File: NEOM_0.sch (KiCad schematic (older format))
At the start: 20 parts, among them U1 LM3940, U2 7_Pins_Header_PA0_PA6, U3 Reset Button, U4 STM32F070F6P6, U6 7_Pins_Header_PA7_PA14, U7 TPD4S012DRYR, U8 16Mhz, U9 USB_Micro_B

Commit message: Updated the PCB unconnected GND pad..
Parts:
- C1: Digi-Key Part Number	 311-1136-1-ND -> (none); DigiKeyPartNumber	 (none) -> 311-1136-1-ND; Manufacturer Part Number	 CC0805KRX7R9BB103 -> (none); ManufacturerPartNumber	 (none) -> CC0805KRX7R9BB103
- C2: Digi-Key Part Number	 490-1691-1-ND -> (none); DigiKeyPartNumber	 (none) -> 490-1691-1-ND; Manufacturer Part Number	 GRM21BR71C105KA01L -> (none); ManufacturerPartNumber	 (none) -> GRM21BR71C105KA01L
- C3: DigiKeyPartNumber (none) -> 490-8319-1-ND; ManufacturerPartNumber	 (none) -> GRM21BR71H474KA88K
- C4: DigiKeyPartNumber	 (none) -> 445-5986-1-ND; ManufacturerPartNumber	 (none) -> C2012X5R0J336M125AC
- C5: Digi-Key Part Number	 478-1395-1-ND -> (none); DigiKeyPartNumber	 (none) -> 478-1395-1-ND; Manufacturer Part Number	 08055C104KAT2A -> (none); ManufacturerPartNumber	 (none) -> 08055C104KAT2A
- D1: Digi-Key Part Number	 67-1557-1-ND -> (none); DigiKeyPartNumber	 (none) -> 67-1557-1-ND; Manufacturer Part Number	 SML-LXR85GC-TR -> (none); ManufacturerPartNumber	 (none) -> SML-LXR85GC-TR
- R1, R4: Digi-Key Part Number	 311-680ARCT-ND -> (none); DigiKeyPartNumber	 (none) -> 311-680ARCT-ND; Manufacturer Part Number	 RC0805JR-07680RL -> (none); ManufacturerPartNumber	 (none) -> RC0805JR-07680RL
- R2: Digi-Key Part Number	 311-100KCRCT-ND -> (none); DigiKeyPartNumber	 (none) -> 311-100KCRCT-ND; Manufacturer Part Number	 RC0805FR-07100KL -> (none); ManufacturerPartNumber	 (none) -> RC0805FR-07100KL
- R3: DigiKeyPartNumber	 (none) -> 311-100KCRCT-ND; ManufacturerPartNumber	 (none) -> RC0805FR-07100KL
- U1: Digi-Key Part Number	 LM3940IMPX-3.3/NOPBCT-ND -> (none); DigiKeyPartNumber	 (none) -> LM3940IMPX-3.3/NOPBCT-ND; Manufacturer Part Number	 LM3940IMPX-3.3/NOPB -> (none); ManufacturerPartNumber	 (none) -> LM3940IMPX-3.3/NOPB
- U2, U6: DigiKeyPartNumber	 (none) -> S1011EC-07-ND; ManufacturerPartNumber	 (none) -> PRPC007SAAN-RC
- U3: Digi-Key Part Number	 EG5353CT-ND -> (none); DigiKeyPartNumber	 (none) -> EG5353CT-ND; Manufacturer Part Number	 TL3305AF260QG -> (none); ManufacturerPartNumber	 (none) -> TL3305AF260QG
- U4: DigiKeyPartNumber	 (none) -> 497-17353-ND; Manufacturer Part Number	 STM32F070F6P6 -> (none); ManufacturerPartNumber	 (none) -> STM32F070F6P6
- U7: DigiKeyPartNumber	 (none) -> 296-24244-1-ND; ManufacturerPartNumber	 (none) -> TPD4S012DRYR
- U8: Digi-Key Part Number	 490-1198-1-ND -> (none); DigiKeyPartNumber	 (none) -> 490-1198-1-ND; Manufacturer Part Number	 CSTCE16M0V53-R0 -> (none); ManufacturerPartNumber	 (none) -> CSTCE16M0V53-R0
- U9: Digi-Key Part Number	 609-4613-1-ND -> (none); DigiKeyPartNumber	 (none) -> 609-4613-1-ND; Manufacturer Part Number	 10118192-0001LF -> (none); ManufacturerPartNumber	 (none) -> 10118192-0001LF

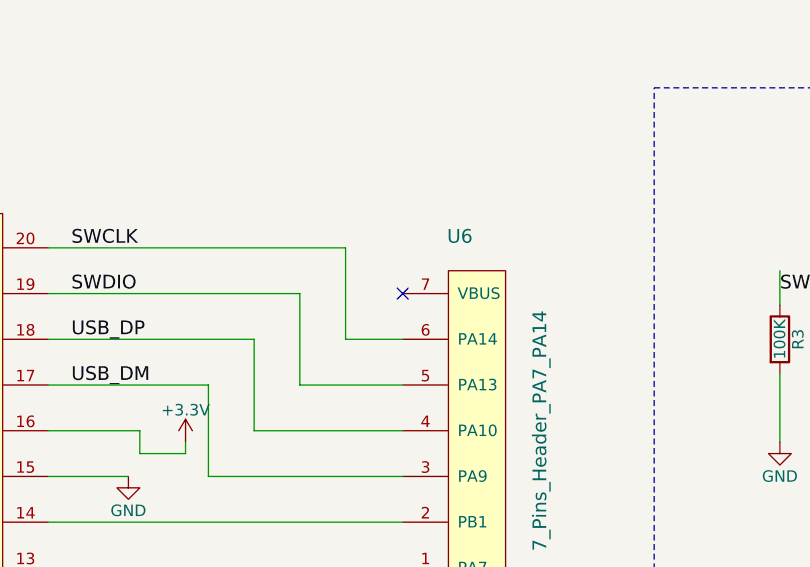
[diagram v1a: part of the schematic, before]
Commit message: Added BAT pin for external battery board..
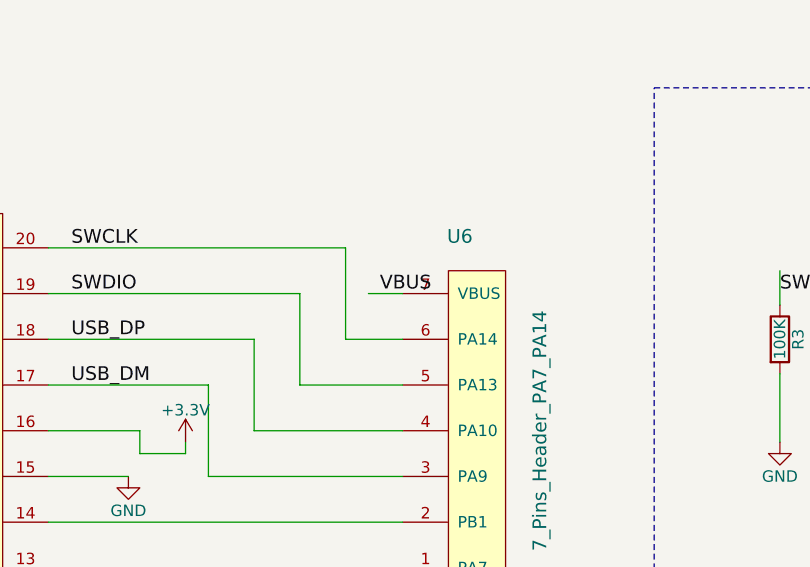
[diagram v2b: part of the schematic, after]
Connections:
- wire segments 88 -> 89
- no-connect marks 2 -> 1
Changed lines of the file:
@@
 Wire Wire Line
 	3350 1400 3200 1400
-NoConn ~ 7800 4200
 $Comp
 L GND #PWR03
@@
 30 3C 9B 92 CF 24 8B DA 51 CD 00 08 DC F9 E9 26 3C 0B 73 01 9F 70 E9 91 80 E7 1F EE EB 72 BD E0
 B4 B1 05 AB 63 DF 09 55 27 EC D5 B5 FC BD 3F 9C 4A 7F 61 62 A3 F8 70 39 5F DC B1 1B B9 9B 02 E2
-5E F0 7F E6 B1 8C 44 57 10 5F 27 00 00 00 00 49 45 4E 44 AE 42 60 82 A3
+5E F0 7F E6 B1 8C 44 57 10 5F 27 00 00 00 00 49 45 4E 44 AE 42 60 82 00
 EndData
 $EndBitmap
@@
 Text Label 9400 1900 1    60   ~ 0
 USB_DM
+Text Label 7700 4200 0    60   ~ 0
+VBUS
+Wire Wire Line
+	7800 4200 7650 4200
 $EndSCHEMATC

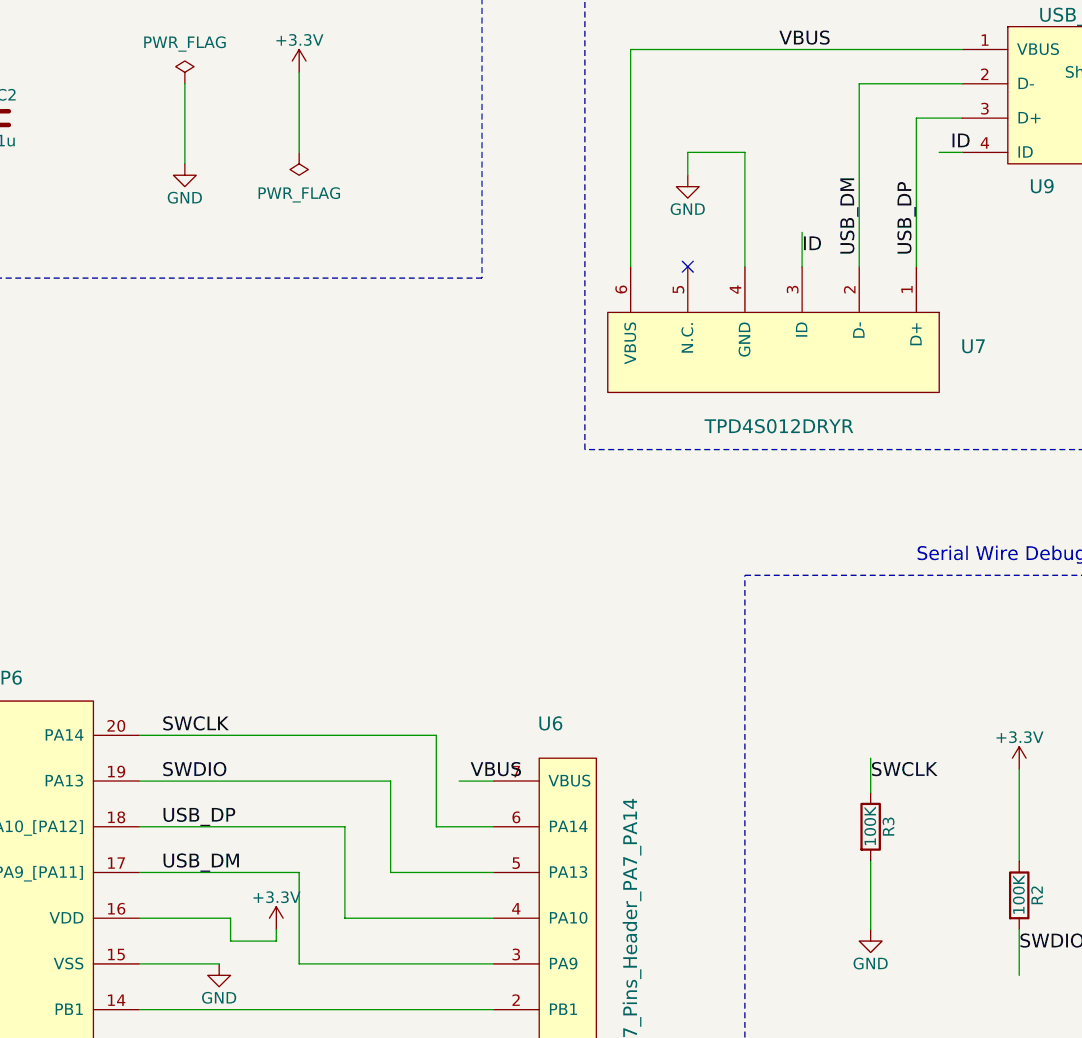
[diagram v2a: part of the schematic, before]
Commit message: Updated PCB: added defferintial pair routing to USB+/-...
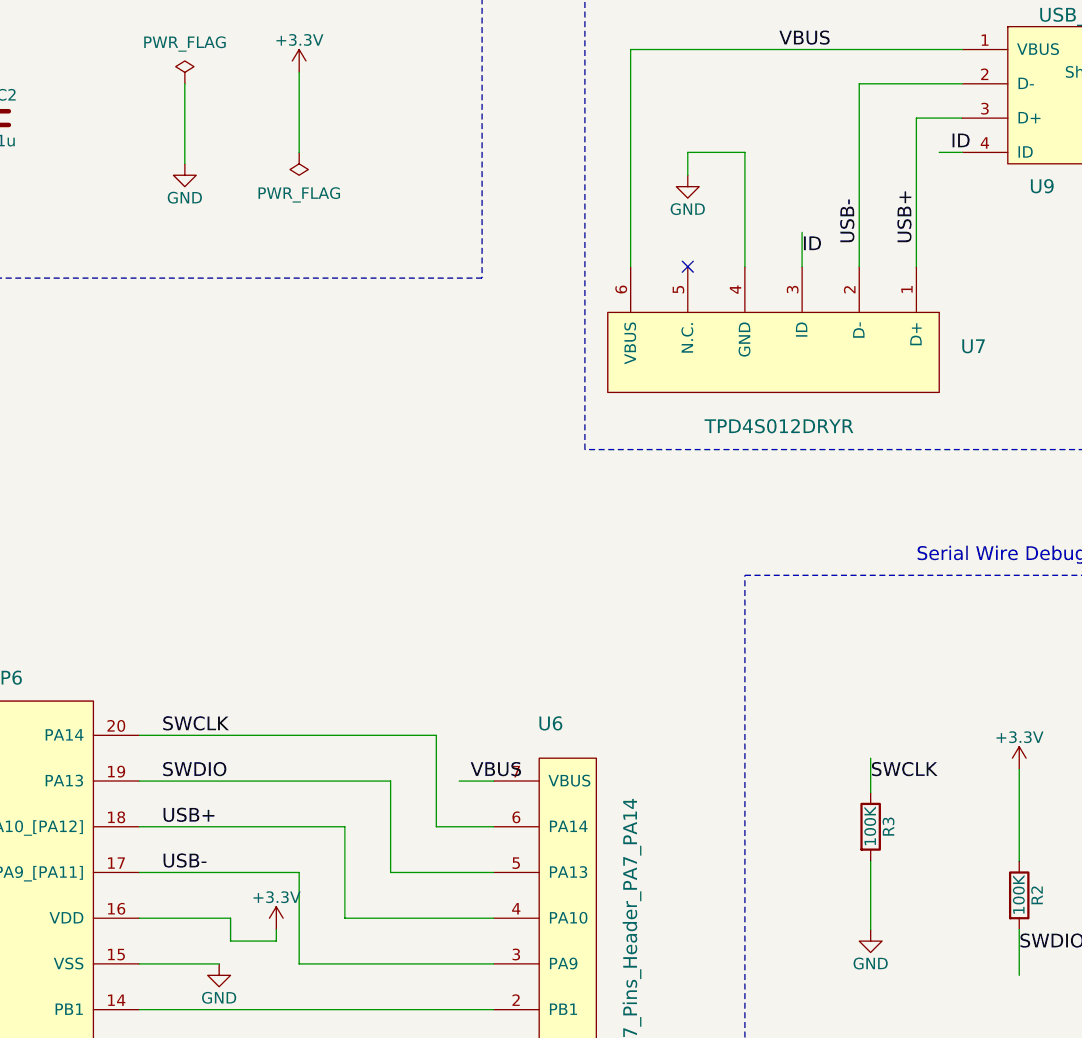
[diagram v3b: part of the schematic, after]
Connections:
- net labels added: USB+, USB-
- net labels removed: USB_DM, USB_DP
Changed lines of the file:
@@
 	9400 1150 9850 1150
-Wire Wire Line
-	9400 1150 9400 1950
 Wire Wire Line
 	9850 1300 9650 1300
@@
 30 3C 9B 92 CF 24 8B DA 51 CD 00 08 DC F9 E9 26 3C 0B 73 01 9F 70 E9 91 80 E7 1F EE EB 72 BD E0
 B4 B1 05 AB 63 DF 09 55 27 EC D5 B5 FC BD 3F 9C 4A 7F 61 62 A3 F8 70 39 5F DC B1 1B B9 9B 02 E2
-5E F0 7F E6 B1 8C 44 57 10 5F 27 00 00 00 00 49 45 4E 44 AE 42 60 82 00
+5E F0 7F E6 B1 8C 44 57 10 5F 27 00 00 00 00 49 45 4E 44 AE 42 60 82 A3
 EndData
 $EndBitmap
@@
 	7750 650  7750 2000
 Text Label 6350 4600 0    60   ~ 0
-USB_DM
+USB-
 Text Label 6350 4400 0    60   ~ 0
-USB_DP
-Text Label 9650 1900 1    60   ~ 0
-USB_DP
-Text Label 9400 1900 1    60   ~ 0
-USB_DM
+USB+
 Text Label 7700 4200 0    60   ~ 0
 VBUS
 Wire Wire Line
 	7800 4200 7650 4200
+Wire Wire Line
+	9400 1150 9400 1950
+Text Label 9650 1850 1    60   ~ 0
+USB+
+Text Label 9400 1850 1    60   ~ 0
+USB-
 $EndSCHEMATC

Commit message: ...
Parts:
- removed C1: 10n, Capacitors_SMD:C_0805, symbol C
- removed C2: 1u, Capacitors_SMD:C_0805, symbol C
- removed C3: 0.47u, Capacitors_SMD:C_0805, symbol C
- removed C4: 33u, Capacitors_SMD:C_0805, symbol C
- removed C5: 0.1u, Capacitors_SMD:C_0805, symbol C
- removed D1: LED, Footprints:0805_LED, symbol LED
- removed FID1, FID2: FIDUCIAL, Footprints2:MF_Aesthetics-FIDUCIAL_100MIL, symbol FIDUCIAL
- removed R1, R4: 680, Resistors_SMD:R_0805, symbol R
- removed R2, R3: 100K, Resistors_SMD:R_0805, symbol R
- removed U1: LM3940, Footprints:LM3940, symbol LM3940
- removed U2: 7_Pins_Header_PA0_PA6, Footprints:7_Pins_Headers, symbol 7_Pins_Header_PA0_PA6
- removed U3: Reset Button, Footprints:Tactile_Button, symbol Tactile_Button
- removed U4: STM32F070F6P6, Footprints:TSSOP20, symbol STM32F070F6P6
- removed U6: 7_Pins_Header_PA7_PA14, Footprints:7_Pins_Headers, symbol 7_Pins_Header_PA7_PA14
- removed U7: TPD4S012DRYR, Footprints:TPD4S012DRYR, symbol TPD4S012DRYR
- removed U8: 16Mhz, Footprints:16Mhz, symbol 16Mhz
- removed U9: USB_Micro_B, Footprints2:MICRO_USB_B_Type, symbol USB_Micro_B
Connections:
- net labels removed: +3.3V, BOOT0, GND, ID, NRST, SWCLK, SWDIO, USB+, USB-, VBUS
- wire segments 89 -> 18
- no-connect marks 1 -> 0
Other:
- note removed: "5v to 3.3v LDO and RESET"
- note removed: "Power Filters and Flags"
- note removed: "Serial Wire Debug - SWD"
- note removed: "USB Connector & ESD"

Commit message: Updated to Rev2.0
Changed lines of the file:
@@
 EESchema Schematic File Version 2
+LIBS:NEOM_0-rescue
 LIBS:power
 LIBS:device
@@
 LIBS:contrib
 LIBS:valves
-LIBS:stm32f070f6p6
 LIBS:tpd4s012dryr
 LIBS:lm3940
 LIBS:tactile_button
+LIBS:NEOM_0
 LIBS:NEOM_0-cache
 EELAYER 25 0
@@
 $Descr A4 11693 8268
 encoding utf-8
-Sheet 1 4
+Sheet 1 5
 Title "NEOM Board Version 0"
 Date "2017-11-17"
@@
 30 3C 9B 92 CF 24 8B DA 51 CD 00 08 DC F9 E9 26 3C 0B 73 01 9F 70 E9 91 80 E7 1F EE EB 72 BD E0
 B4 B1 05 AB 63 DF 09 55 27 EC D5 B5 FC BD 3F 9C 4A 7F 61 62 A3 F8 70 39 5F DC B1 1B B9 9B 02 E2
-5E F0 7F E6 B1 8C 44 57 10 5F 27 00 00 00 00 49 45 4E 44 AE 42 60 82 00
+5E F0 7F E6 B1 8C 44 57 10 5F 27 00 00 00 00 49 45 4E 44 AE 42 60 82
 EndData
 $EndBitmap
 $Sheet
-S 2550 1600 1950 950
+S 1950 3350 1950 950
 U 5A19D99A
 F0 "Power_Managment" 60
 F1 "Power_Managment.sch" 60
-F2 "NRST" I R 4500 2100 60
-F3 "VBUS" I L 2550 2000 60
-F4 "+3.3v" I R 4500 1750 60
+F2 "NRST" I R 3900 3850 60
+F3 "VBUS" I L 1950 3750 60
+F4 "+3.3v" I R 3900 3500 60
 $EndSheet
 $Sheet
-S 8100 1700 1800 900
+S 7800 4000 1800 900
 U 5A19F5EA
 F0 "USB" 60
 F1 "USB.sch" 60
-F2 "USB-" I L 8100 1900 60
-F3 "USB+" I L 8100 2150 60
-F4 "VBUS" I L 8100 2350 60
+F2 "USB-" I L 7800 4200 60
+F3 "USB+" I L 7800 4400 60
+F4 "VBUS" I L 7800 4600 60
 $EndSheet
 $Sheet
-S 4950 3600 2400 1200
+S 4500 3050 2400 1700
 U 5A19FC34
-F0 "STM32F070F6P6" 60
-F1 "STM32F070F6P6.sch" 60
-F2 "NRST" I L 4950 4400 60
-F3 "+3.3v" I L 4950 4100 60
-F4 "USB+" I R 7350 4200 60
-F5 "USB-" I R 7350 3950 60
-F6 "VBUS" I R 7350 4500 60
+F0 "STM32F401CEU6" 60
+F1 "STM32F401CEU6.sch" 60
+F2 "NRST" I L 4500 3850 60
+F3 "+3.3v" I L 4500 3500 60
+F4 "USB+" I R 6900 4400 60
+F5 "USB-" I R 6900 4200 60
+F6 "VBUS" I R 6900 4600 60
+F7 "UART_CTS" I R 6900 3800 60
+F8 "UART_RTS" I R 6900 3600 60
+F9 "UART_RX" I R 6900 3400 60
+F10 "UART_TX" I R 6900 3200 60
 $EndSheet
-Wire Wire Line
-	2550 2000 2150 2000
-Wire Wire Line
-	2150 2000 2150 5300
-Wire Wire Line
-	2150 5300 7700 5300
-Wire Wire Line
-	7700 5300 7700 2350
-Wire Wire Line
-	7700 4500 7350 4500
-Wire Wire Line
-	7700 2350 8100 2350
-Connection ~ 7700 4500
-Wire Wire Line
-	4950 4100 4800 4100
-Wire Wire Line
-	4800 4100 4800 1750
-Wire Wire Line
-	4800 1750 4500 1750
-Wire Wire Line
-	4500 2100 4600 2100
-Wire Wire Line
-	4600 2100 4600 4400
-Wire Wire Line
-	4600 4400 4950 4400
-Wire Wire Line
-	7350 4200 7600 4200
-Wire Wire Line
-	7600 4200 7600 2150
-Wire Wire Line
-	7600 2150 8100 2150
-Wire Wire Line
-	8100 1900 7500 1900
-Wire Wire Line
-	7500 1900 7500 3950
-Wire Wire Line
-	7500 3950 7350 3950
+$Sheet
+S 4500 1500 2000 900
+U 5A360125
+F0 "Wireless_AMW007R" 60
+F1 "AMW007R.sch" 60
+F2 "UART_TX" I R 6500 2250 60
+F3 "UART_RX" I R 6500 2050 60
+F4 "UART_CTS" I R 6500 1650 60
+F5 "UART_RTS" I R 6500 1850 60
+F6 "+3.3v" I L 4500 1800 60
+$EndSheet
+Wire Wire Line
+	1950 3750 1700 3750
+Wire Wire Line
+	1700 3750 1700 5100
+Wire Wire Line
+	4500 1800 4150 1800
+Wire Wire Line
+	3900 3850 4500 3850
+Wire Wire Line
+	3900 3500 4500 3500
+Wire Wire Line
+	4150 1800 4150 3500
+Connection ~ 4150 3500
+Wire Wire Line
+	6900 3200 7050 3200
+Wire Wire Line
+	7050 3200 7050 2250
+Wire Wire Line
+	7050 2250 6500 2250
+Wire Wire Line
+	6500 2050 7200 2050
+Wire Wire Line
+	7200 2050 7200 3400
+Wire Wire Line
+	7200 3400 6900 3400
+Wire Wire Line
+	6900 3600 7350 3600
+Wire Wire Line
+	7350 3600 7350 1850
+Wire Wire Line
+	7350 1850 6500 1850
+Wire Wire Line
+	6500 1650 7450 1650
+Wire Wire Line
+	7450 1650 7450 3800
+Wire Wire Line
+	7450 3800 6900 3800
+Wire Wire Line
+	7800 4200 6900 4200
+Wire Wire Line
+	6900 4400 7800 4400
+Wire Wire Line
+	7800 4600 6900 4600
+Wire Wire Line
+	1700 5100 7400 5100
+Wire Wire Line
+	7400 5100 7400 4600
+Connection ~ 7400 4600
 $EndSCHEMATC
